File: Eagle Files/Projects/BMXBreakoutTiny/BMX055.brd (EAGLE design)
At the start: 7 x 15.9 mm, 4 parts, among them U1 BMX055

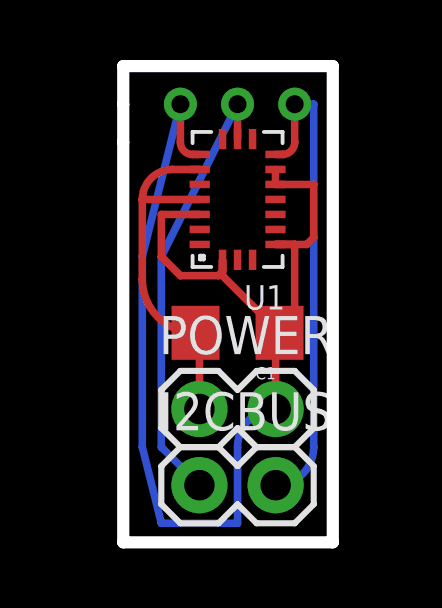
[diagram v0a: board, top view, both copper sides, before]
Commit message: Adjusted to take advantage of OSHPark guidelines
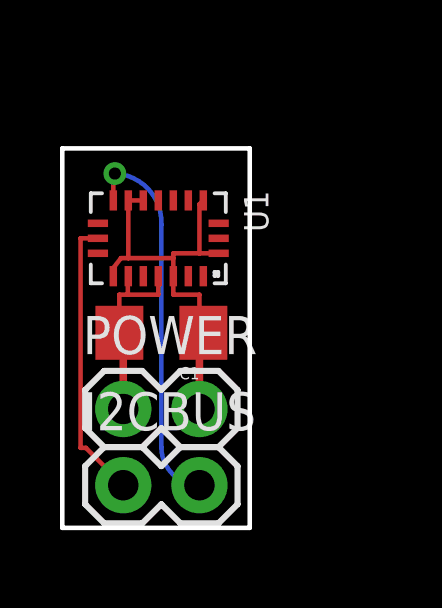
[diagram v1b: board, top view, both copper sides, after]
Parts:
- moved U1 2.94 mm to (2.44, 9.50), turned to 270 degrees
- moved C1 2.54 mm to (2.54, 6.35)
- moved I2CBUS 2.54 mm to (1.27, 1.27)
- moved POWER 2.54 mm to (1.27, 3.81)
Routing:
- net VDD: track 43.5 -> 14.4 mm, vias 1 -> 0
- net GND: track 12.1 -> 6.49 mm
- net N$1: track 15.0 -> 9.50 mm, vias 1 -> 0
- net N$2: track 15.9 -> 12.5 mm
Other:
- board size 7 x 15.9 mm -> 6.2 x 12.6 mm
